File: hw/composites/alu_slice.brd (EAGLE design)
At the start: 50 x 50 mm, 12 parts

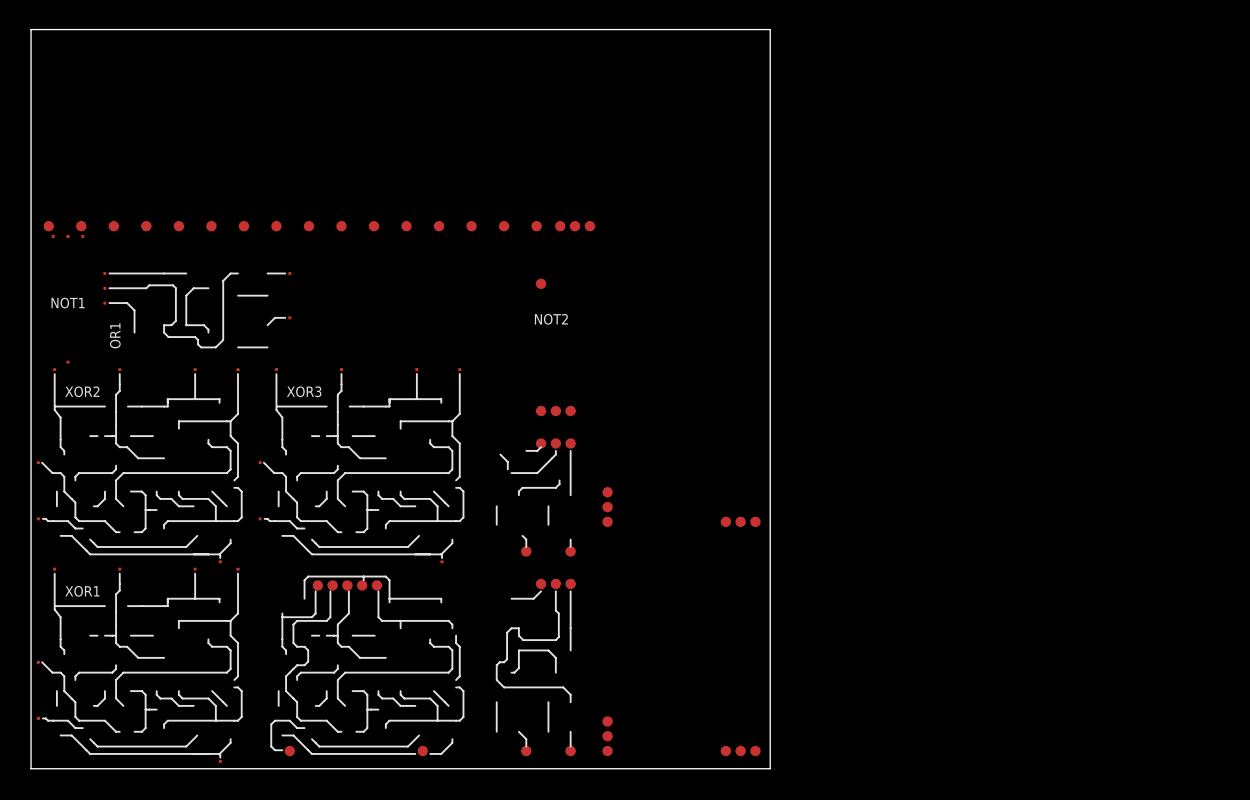
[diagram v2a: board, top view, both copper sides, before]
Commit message: Migrated alu to new format
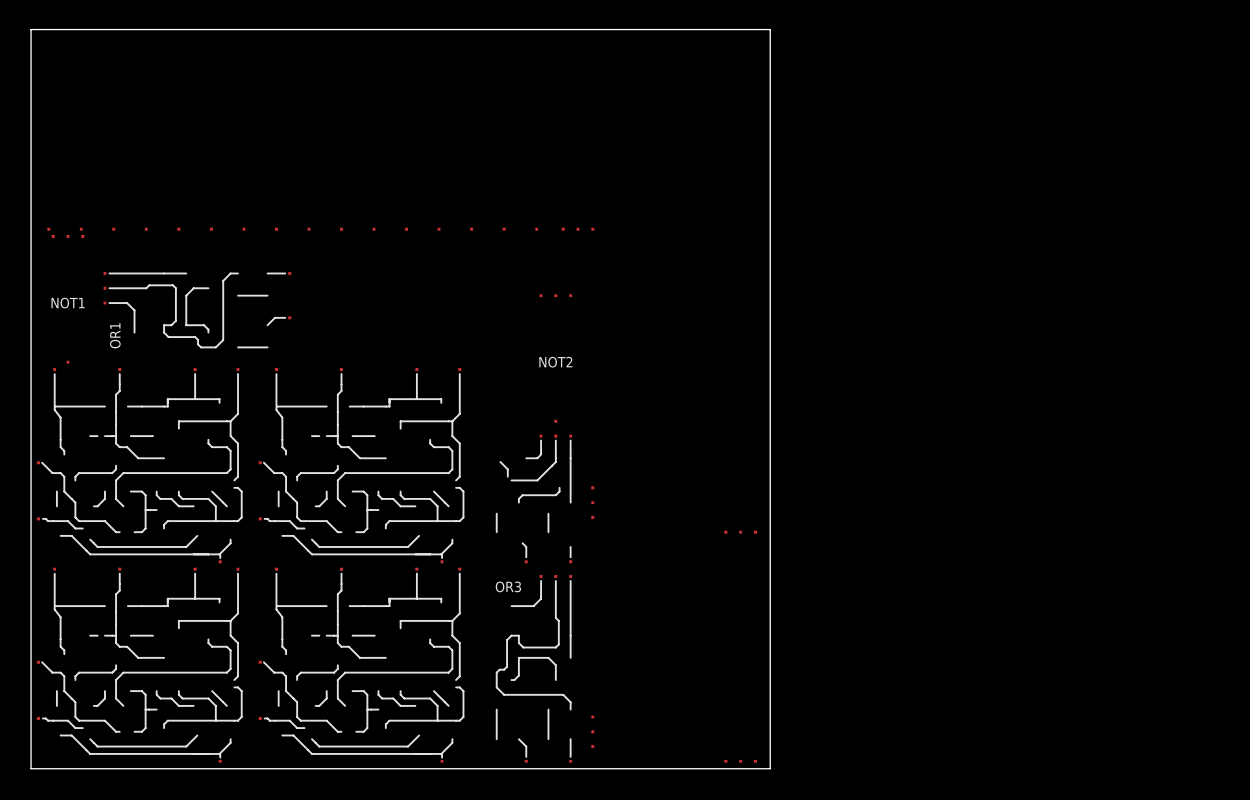
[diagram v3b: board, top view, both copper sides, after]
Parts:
- removed OR2: OR, p.peter-logic:OR-2
- added OR3: OR, p.peter-gator:OR
- NAND1: device p.peter-logic:NAND-2 -> p.peter-gator:NAND
- NOT2: value NOT-VERTICAL -> NOTVERTICAL; device p.peter-logic:NOT-VERTICAL -> p.peter-gator:NOT-VERTICAL
- SEL1: value SELECTOR -> 1_BIT_SELECT; device p.peter-logic:SELECTOR-8_BIT-NOMUX -> p.peter-gator:SELECTOR-2-LANE-NOMUX
- SEL2: value (none) -> 8_BIT_SELECT; device p.peter-logic:SELECTOR-2-LANE-NOMUX -> p.peter-gator:SELECTOR-8_BIT-NOMUX
- SEL3: value (none) -> 1_BIT_SELECT; device p.peter-logic:SELECTOR-2-LANE-NOMUX -> p.peter-gator:SELECTOR-2-LANE-NOMUX
- XOR4: device p.peter-logic:XOR-2-EX2 -> p.peter-gator:XOR
- moved SEL2 43.2 mm to (0.00, 36.5)
- moved SEL1 42.9 mm to (38.0, 16.0)
- moved XOR4 9.74 mm to (15.5, 0.50)
- moved NAND1 5.70 mm to (30.5, 14.0)
- moved NOT2 5.39 mm to (33.5, 23.5), turned to 0 degrees
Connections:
- removed net N$3: SEL1.IN6, SEL2.OUT
- removed net N$4: NAND1.OUT2, XOR4.B
- removed net N$5: NAND1.B, NOT2.OUT1
- removed net OUT: SEL1.OUT, XOR4.A
- removed net OUT_INV: XOR4.OUT4
- removed net SEL_ADD: SEL1.SEL5
- removed net SEL_AND: SEL1.SEL2
- removed net SEL_CMP: SEL1.SEL7, SEL3.SEL
- removed net SEL_ID: SEL1.SEL1
- removed net SEL_LOAD: SEL1.SEL8
- removed net SEL_OR: SEL1.SEL3
- removed net SEL_SHIFT: NAND1.A, SEL1.SEL6
- removed net SEL_XOR: SEL1.SEL4
- new net N$1: NAND1.NAND, XOR4.B
- new net N$2: SEL1.OUT, SEL2.I6
- new net N$7: NAND1.A, NOT2.NOT
- new net S_ADD: SEL2.S5
- new net S_AND: SEL2.S2
- new net S_CMP: SEL2.S7, SEL3.SEL
- new net S_ID: SEL2.S1
- new net S_LOAD: SEL2.S8
- new net S_NOR: SEL2.S3
- new net S_SHIFT: NAND1.B, SEL2.S6
- new net S_XOR: SEL2.S4
- net +5V: now also NAND1.V+, NOT2.V+, OR3.V+, SEL1.V+, SEL2.V+, SEL3.V+, XOR4.V+
- net A: now also SEL2.I1, SEL3.B; no longer SEL1.IN1, SEL3.IN2
- net B: now also SEL2.I8; no longer SEL1.IN8
- net EQUAL_IN: now also OR3.B; no longer OR2.B
- net EQUAL_OUT: now also OR3.OR; no longer OR2.OUT1
- net GND: now also NAND1.V-, NOT2.V-, OR3.V-, SEL1.V-, SEL2.V-, SEL3.V-, XOR4.V-
- net INV_OUT: now also NOT2.A, SEL1.SEL; no longer NOT2.IN, SEL2.SEL
- net LEFT_IN: now also SEL1.A, SEL2.I7, SEL3.A; no longer SEL1.IN7, SEL2.IN1, SEL3.IN1
- net NAND: now also SEL2.I2; no longer SEL1.IN2
- net NOR: now also SEL2.I3; no longer SEL1.IN3
- net RIGHT_IN: now also SEL1.B; no longer SEL2.IN2
- net SUM: now also OR3.A, SEL2.I5; no longer OR2.A, SEL1.IN5
- net XOR: now also SEL2.I4; no longer SEL1.IN4

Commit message: Started on ALU
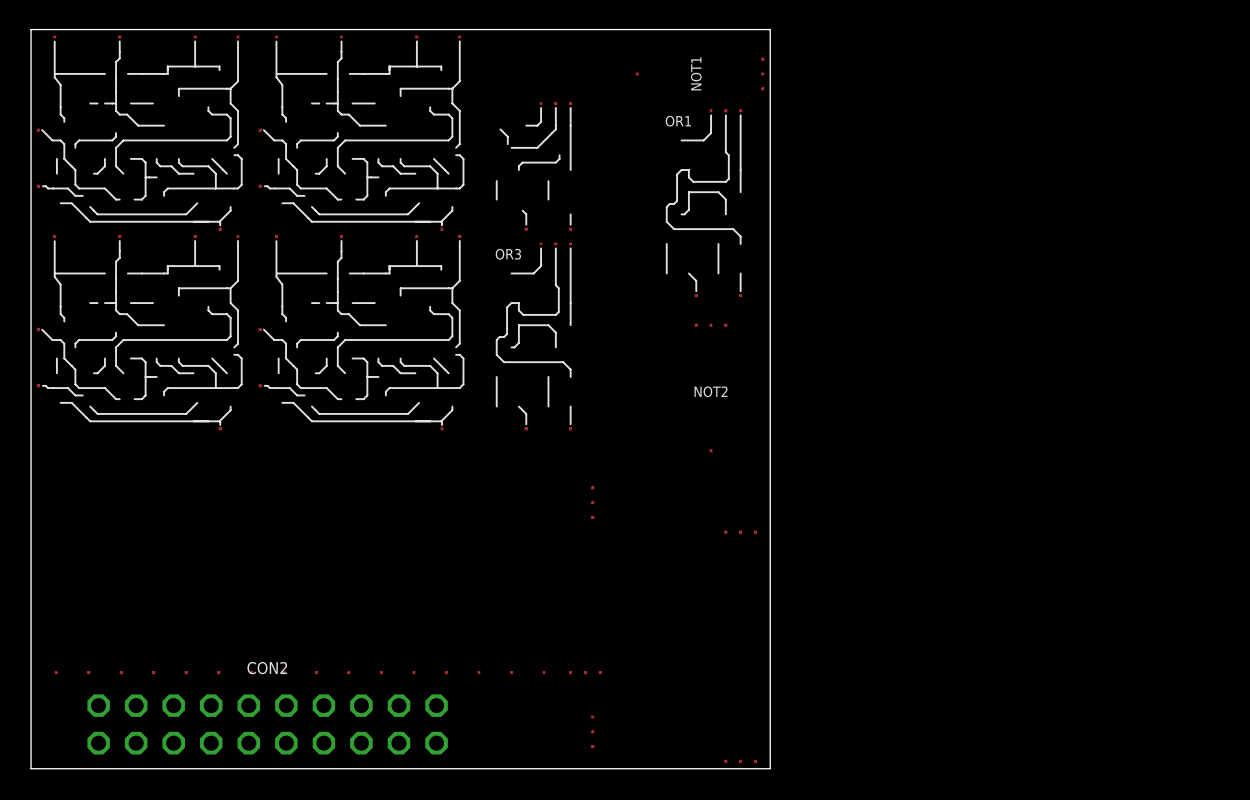
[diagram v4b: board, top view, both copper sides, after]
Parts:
- added CON2: (no value), p.peter-connectors:PINHEADER-100MIL-2X10-NOSILK
- moved NOT1 45.9 mm to (41.0, 49.0), turned to 270 degrees
- moved SEL2 30.0 mm to (0.50, 6.50)
- moved OR1 24.9 mm to (42.0, 32.0), turned to 0 degrees
- moved NAND1 22.5 mm to (30.5, 36.5)
- moved OR3 22.5 mm to (30.5, 23.0)
- moved XOR1 22.5 mm to (0.50, 23.0)
- moved XOR2 22.5 mm to (0.50, 36.5)
- moved XOR3 22.5 mm to (15.5, 36.5)
- moved XOR4 22.5 mm to (15.5, 23.0)
- moved NOT2 10.7 mm to (44.0, 21.5)
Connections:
- new net N$3: SEL2.OUT, XOR4.A
- new net OVERFLOW: CON2.17
- new net RESULT: CON2.11, XOR4.XOR
- net +5V: now also CON2.2
- net A: now also CON2.1
- net B: now also CON2.3
- net CARRY: now also CON2.15
- net EQUAL_IN: now also CON2.9
- net EQUAL_OUT: now also CON2.19
- net GND: now also CON2.20
- net LEFT_IN: now also CON2.5
- net RIGHT_IN: now also CON2.7
- net RIGHT_OUT: now also CON2.13
- net S_ADD: now also CON2.12
- net S_AND: now also CON2.6
- net S_CMP: now also CON2.16
- net S_ID: now also CON2.4
- net S_LOAD: now also CON2.18
- net S_NOR: now also CON2.8
- net S_SHIFT: now also CON2.14
- net S_XOR: now also CON2.10

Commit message: Updated supply line names to be more spice compatible
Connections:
- net +5V: now also NAND1._VP, NOT1._VP, NOT2._VP, OR1._VP, OR3._VP, SEL1._VP, SEL2._VP, SEL3._VP, XOR1._VP, XOR2._VP, XOR3._VP, XOR4._VP; no longer NAND1.V+, NOT1.V+, NOT2.V+, OR1.V+, OR3.V+, SEL1.V+, SEL2.V+, SEL3.V+, XOR1.V+, XOR2.V+, XOR3.V+, XOR4.V+
- net GND: now also NAND1._VN, NOT1._VN, NOT2._VN, OR1._VN, OR3._VN, SEL1._VN, SEL2._VN, SEL3._VN, XOR1._VN, XOR2._VN, XOR3._VN, XOR4._VN; no longer NAND1.V-, NOT1.V-, NOT2.V-, OR1.V-, OR3.V-, SEL1.V-, SEL2.V-, SEL3.V-, XOR1.V-, XOR2.V-, XOR3.V-, XOR4.V-
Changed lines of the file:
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@@
 <?xml version="1.0" encoding="utf-8"?>
 <!DOCTYPE eagle SYSTEM "eagle.dtd">
-<eagle version="7.4.0">
+<eagle version="7.3.0">
 <drawing>
 <settings>
@@
 </signal>
 <signal name="+5V">
-<contactref element="XOR1" pad="V+"/>
-<contactref element="XOR2" pad="V+"/>
-<contactref element="NOT1" pad="V+"/>
-<contactref element="XOR3" pad="V+"/>
-<contactref element="OR1" pad="V+"/>
-<contactref element="OR3" pad="V+"/>
-<contactref element="SEL2" pad="V+"/>
-<contactref element="SEL1" pad="V+"/>
-<contactref element="SEL3" pad="V+"/>
-<contactref element="NOT2" pad="V+"/>
-<contactref element="NAND1" pad="V+"/>
-<contactref element="XOR4" pad="V+"/>
+<contactref element="XOR1" pad="_VP"/>
+<contactref element="XOR2" pad="_VP"/>
+<contactref element="NOT1" pad="_VP"/>
+<contactref element="XOR3" pad="_VP"/>
+<contactref element="OR1" pad="_VP"/>
+<contactref element="OR3" pad="_VP"/>
+<contactref element="SEL2" pad="_VP"/>
+<contactref element="SEL1" pad="_VP"/>
+<contactref element="SEL3" pad="_VP"/>
+<contactref element="NOT2" pad="_VP"/>
+<contactref element="NAND1" pad="_VP"/>
+<contactref element="XOR4" pad="_VP"/>
 <contactref element="CON2" pad="2"/>
 <wire x1="48" y1="44.5" x2="49.5" y2="46" width="0" layer="19" extent="1-1"/>
@@
 </signal>
 <signal name="GND">
-<contactref element="XOR1" pad="V-"/>
-<contactref element="XOR2" pad="V-"/>
-<contactref element="NOT1" pad="V-"/>
-<contactref element="XOR3" pad="V-"/>
-<contactref element="OR1" pad="V-"/>
-<contactref element="OR3" pad="V-"/>
-<contactref element="SEL1" pad="V-"/>
-<contactref element="SEL2" pad="V-"/>
-<contactref element="SEL3" pad="V-"/>
-<contactref element="NOT2" pad="V-"/>
-<contactref element="NAND1" pad="V-"/>
-<contactref element="XOR4" pad="V-"/>
+<contactref element="XOR1" pad="_VN"/>
+<contactref element="XOR2" pad="_VN"/>
+<contactref element="NOT1" pad="_VN"/>
+<contactref element="XOR3" pad="_VN"/>
+<contactref element="OR1" pad="_VN"/>
+<contactref element="OR3" pad="_VN"/>
+<contactref element="SEL1" pad="_VN"/>
+<contactref element="SEL2" pad="_VN"/>
+<contactref element="SEL3" pad="_VN"/>
+<contactref element="NOT2" pad="_VN"/>
+<contactref element="NAND1" pad="_VN"/>
+<contactref element="XOR4" pad="_VN"/>
 <contactref element="CON2" pad="20"/>
 <wire x1="47" y1="44.5" x2="49.5" y2="47" width="0" layer="19" extent="1-1"/>

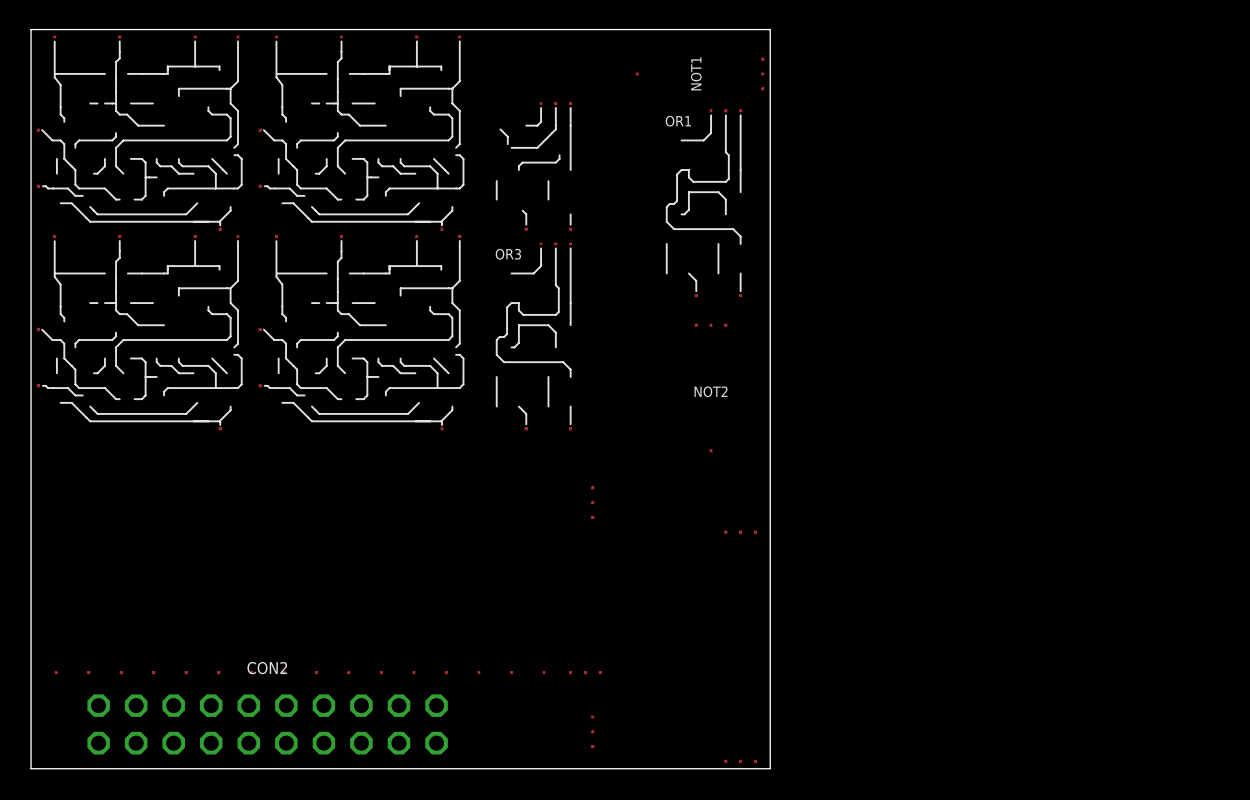
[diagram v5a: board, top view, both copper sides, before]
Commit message: Trying to mimize gates some more
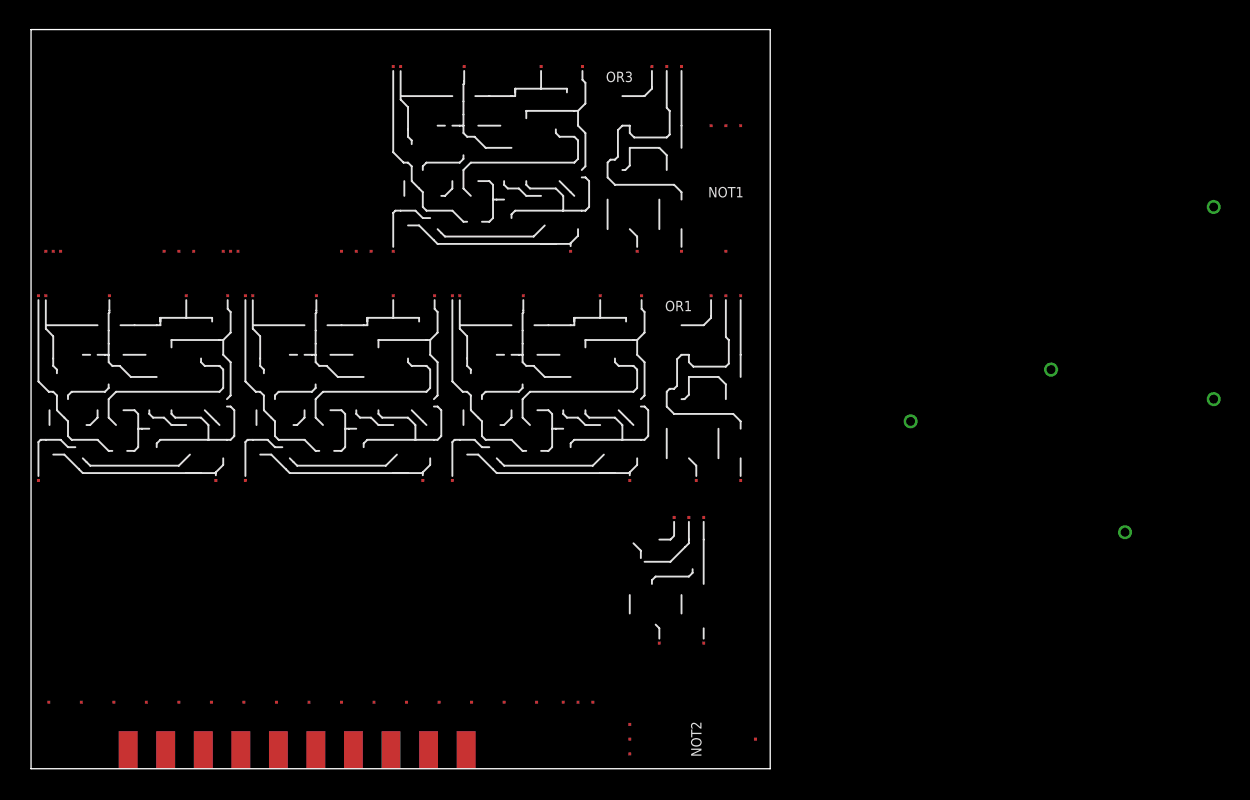
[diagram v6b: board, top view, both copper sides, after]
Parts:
- CON2: value (none) -> GENERIC-2X10; device p.peter-connectors:PINHEADER-100MIL-2X10-NOSILK -> p.peter-connectors:PINHEADER-100MIL-2X10-EDGE
- moved SEL3 43.2 mm to (12.0, 35.0)
- moved SEL1 42.5 mm to (0.00, 35.0)
- moved NAND1 29.4 mm to (39.5, 8.50)
- moved XOR2 23.5 mm to (24.0, 35.0)
- moved NOT2 22.1 mm to (49.0, 0.00), turned to 90 degrees
- moved XOR3 21.1 mm to (28.0, 19.5)
- moved XOR4 15.9 mm to (0.00, 19.5)
- moved NOT1 14.6 mm to (45.0, 35.0), turned to 0 degrees
- moved OR3 14.2 mm to (38.0, 35.0)
- moved XOR1 13.9 mm to (14.0, 19.5)
- moved OR1 12.5 mm to (42.0, 19.5)
- moved CON2 3.61 mm to (18.0, 0.00)
- moved SEL2 2.06 mm to (0.00, 4.50)
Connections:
- net +5V: now also NAND1.V+, NOT1.V+, NOT2.V+, OR1.V+, OR3.V+, SEL1.V+, SEL2.V+, SEL3.V+, XOR1.V+, XOR2.V+, XOR3.V+, XOR4.V+; no longer NAND1._VP, NOT1._VP, NOT2._VP, OR1._VP, OR3._VP, SEL1._VP, SEL2._VP, SEL3._VP, XOR1._VP, XOR2._VP, XOR3._VP, XOR4._VP
- net GND: now also NAND1.V-, NOT1.V-, NOT2.V-, OR1.V-, OR3.V-, SEL1.V-, SEL2.V-, SEL3.V-, XOR1.V-, XOR2.V-, XOR3.V-, XOR4.V-; no longer NAND1._VN, NOT1._VN, NOT2._VN, OR1._VN, OR3._VN, SEL1._VN, SEL2._VN, SEL3._VN, XOR1._VN, XOR2._VN, XOR3._VN, XOR4._VN

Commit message: Fixing stuff
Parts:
- moved NOT1 0.71 mm to (45.5, 34.5)
- moved OR3 0.71 mm to (38.5, 34.5)
- moved SEL1 0.71 mm to (0.50, 34.5)
- moved SEL3 0.71 mm to (12.5, 34.5)
- moved XOR2 0.71 mm to (24.5, 34.5)
- moved NAND1 0.50 mm to (40.0, 8.50)
- moved OR1 0.50 mm to (42.5, 19.5)
- moved SEL2 0.50 mm to (0.50, 4.50)
- moved XOR1 0.50 mm to (14.5, 19.5)
- moved XOR3 0.50 mm to (28.5, 19.5)
- moved XOR4 0.50 mm to (0.50, 19.5)
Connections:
- net +5V: now also NAND1._VP, NOT1._VP, NOT2._VP, OR1._VP, OR3._VP, SEL1._VP, SEL2._VP, SEL3._VP, XOR1._VP, XOR2._VP, XOR3._VP, XOR4._VP; no longer NAND1.V+, NOT1.V+, NOT2.V+, OR1.V+, OR3.V+, SEL1.V+, SEL2.V+, SEL3.V+, XOR1.V+, XOR2.V+, XOR3.V+, XOR4.V+
- net GND: now also NAND1._VN, NOT1._VN, NOT2._VN, OR1._VN, OR3._VN, SEL1._VN, SEL2._VN, SEL3._VN, XOR1._VN, XOR2._VN, XOR3._VN, XOR4._VN; no longer NAND1.V-, NOT1.V-, NOT2.V-, OR1.V-, OR3.V-, SEL1.V-, SEL2.V-, SEL3.V-, XOR1.V-, XOR2.V-, XOR3.V-, XOR4.V-

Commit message: reordering board
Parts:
- moved NOT2 40.0 mm to (9.00, 0.50)
- moved NAND1 39.7 mm to (0.50, 5.00)
- moved XOR4 28.0 mm to (28.5, 19.5)
- moved XOR2 18.8 mm to (38.5, 47.0), turned to 180 degrees
- moved XOR1 14.0 mm to (0.50, 19.5)
- moved XOR3 14.0 mm to (14.5, 19.5)
- moved CON2 10.5 mm to (28.5, 0.00)
- moved SEL2 9.51 mm to (10.0, 5.00)
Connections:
- net +5V: now also CON2.19; no longer CON2.2
- net A: now also CON2.10, SEL2.I4; no longer CON2.1, SEL2.I1
- net B: now also SEL2.I2; no longer SEL2.I8
- net CARRY: now also CON2.11; no longer CON2.15
- net EQUAL_IN: now also CON2.13; no longer CON2.9
- net EQUAL_OUT: now also CON2.17; no longer CON2.19
- net LEFT_IN: now also CON2.7, SEL2.I3; no longer CON2.5, SEL2.I7
- net N$2: now also SEL2.I1; no longer SEL2.I6
- net NAND: now also SEL2.I8; no longer SEL2.I2
- net NOR: now also SEL2.I7; no longer SEL2.I3
- net OVERFLOW: now also CON2.5; no longer CON2.17
- net RESULT: now also CON2.15; no longer CON2.11
- net RIGHT_IN: now also CON2.1; no longer CON2.7
- net RIGHT_OUT: now also CON2.9; no longer CON2.13
- net S_AND: now also CON2.18, SEL2.S8; no longer CON2.6, SEL2.S2
- net S_CMP: now also CON2.6, SEL2.S3; no longer CON2.16, SEL2.S7
- net S_ID: now also CON2.8, SEL2.S4; no longer CON2.4, SEL2.S1
- net S_LOAD: now also CON2.4, SEL2.S2; no longer CON2.18, SEL2.S8
- net S_NOR: now also CON2.16, SEL2.S7; no longer CON2.8, SEL2.S3
- net S_SHIFT: now also CON2.2, SEL2.S1; no longer CON2.14, SEL2.S6
- net S_XOR: now also CON2.14, SEL2.S6; no longer CON2.10, SEL2.S4
- net XOR: now also SEL2.I6; no longer SEL2.I4
